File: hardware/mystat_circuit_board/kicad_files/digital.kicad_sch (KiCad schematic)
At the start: 28 parts, among them J2 2173157-3, P1 ICSP, U5 PIC16F1459, U6 ADR421, U7 MCP3551, U8 MCP3551, U9 DAC1220, X1 2.5 MHz

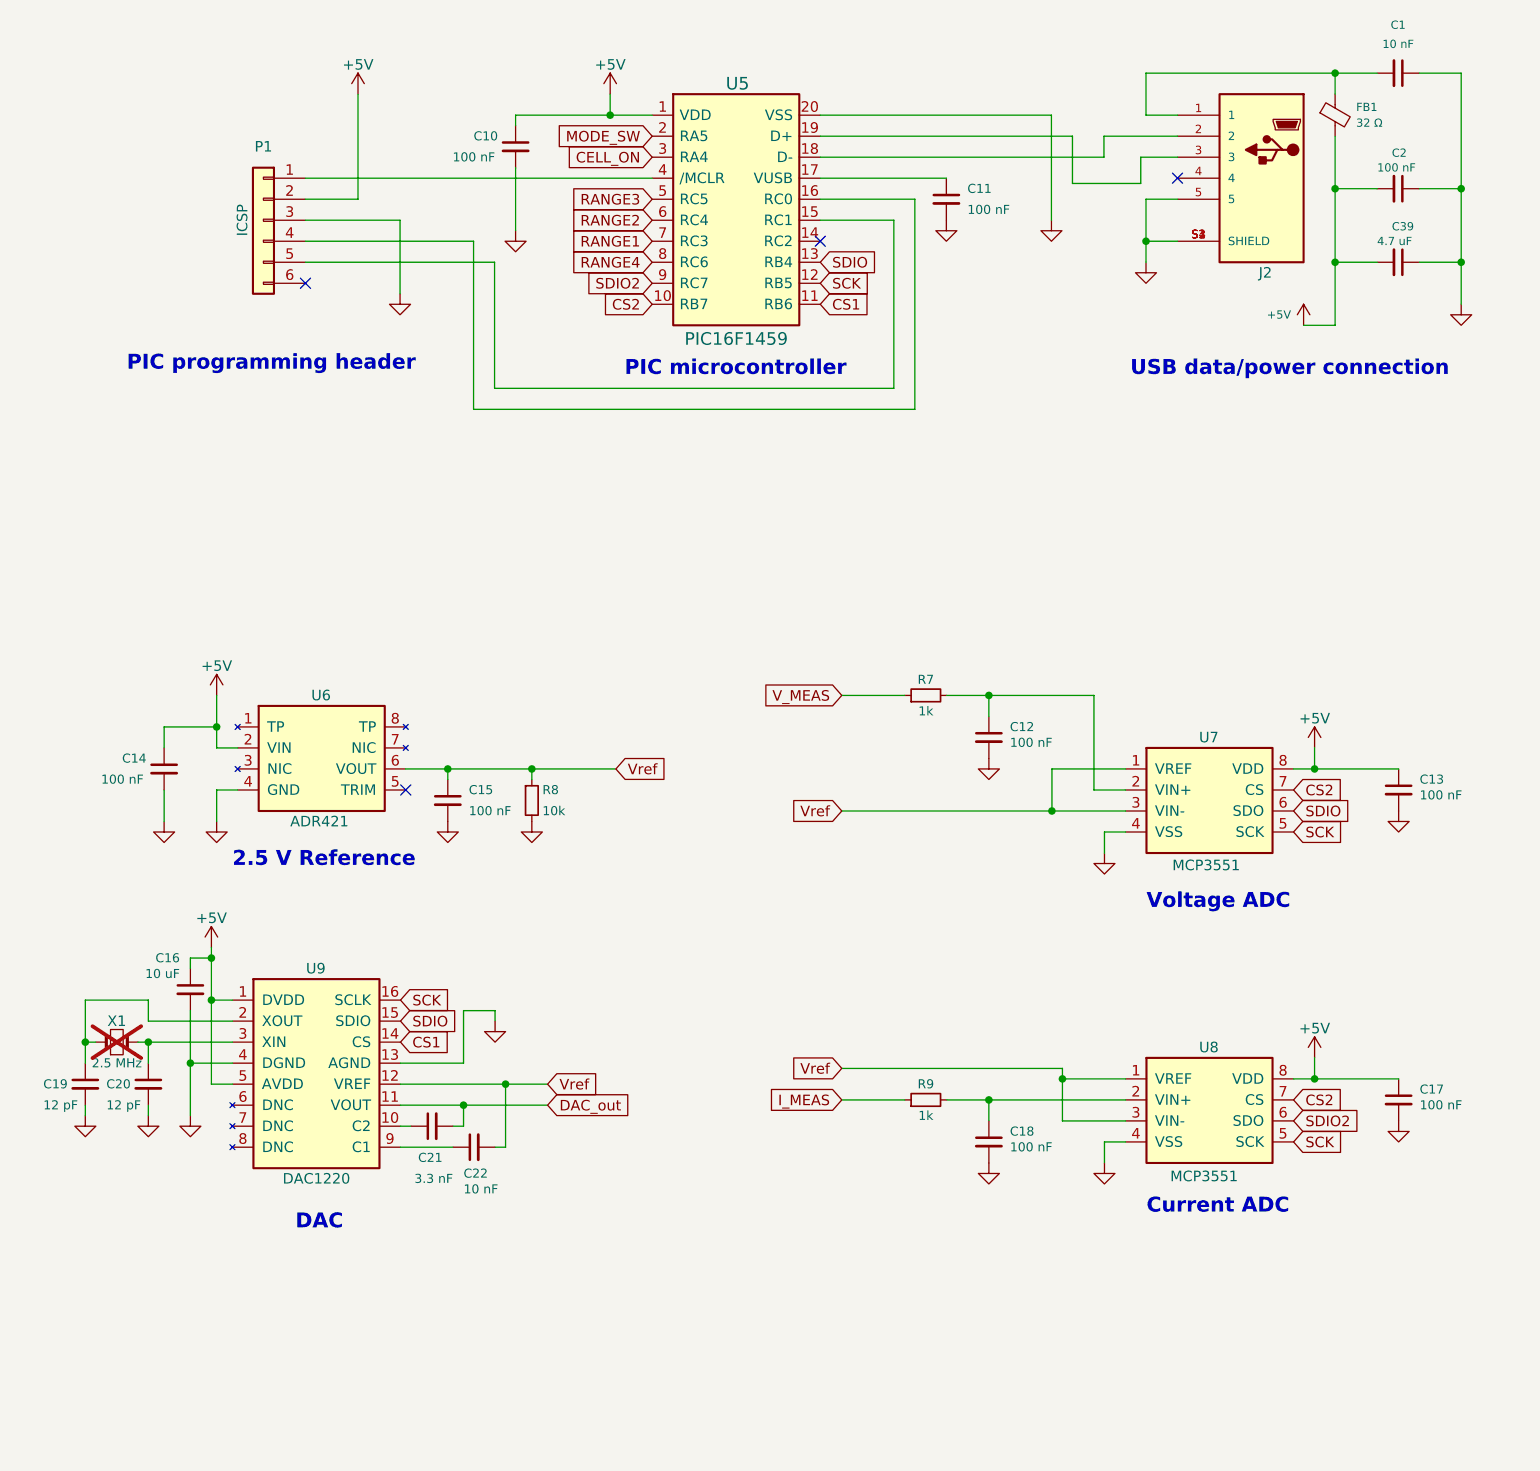
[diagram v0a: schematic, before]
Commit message: change micro USB to USB C 16P 2.0, rotate U11 for routing of thermal pad version
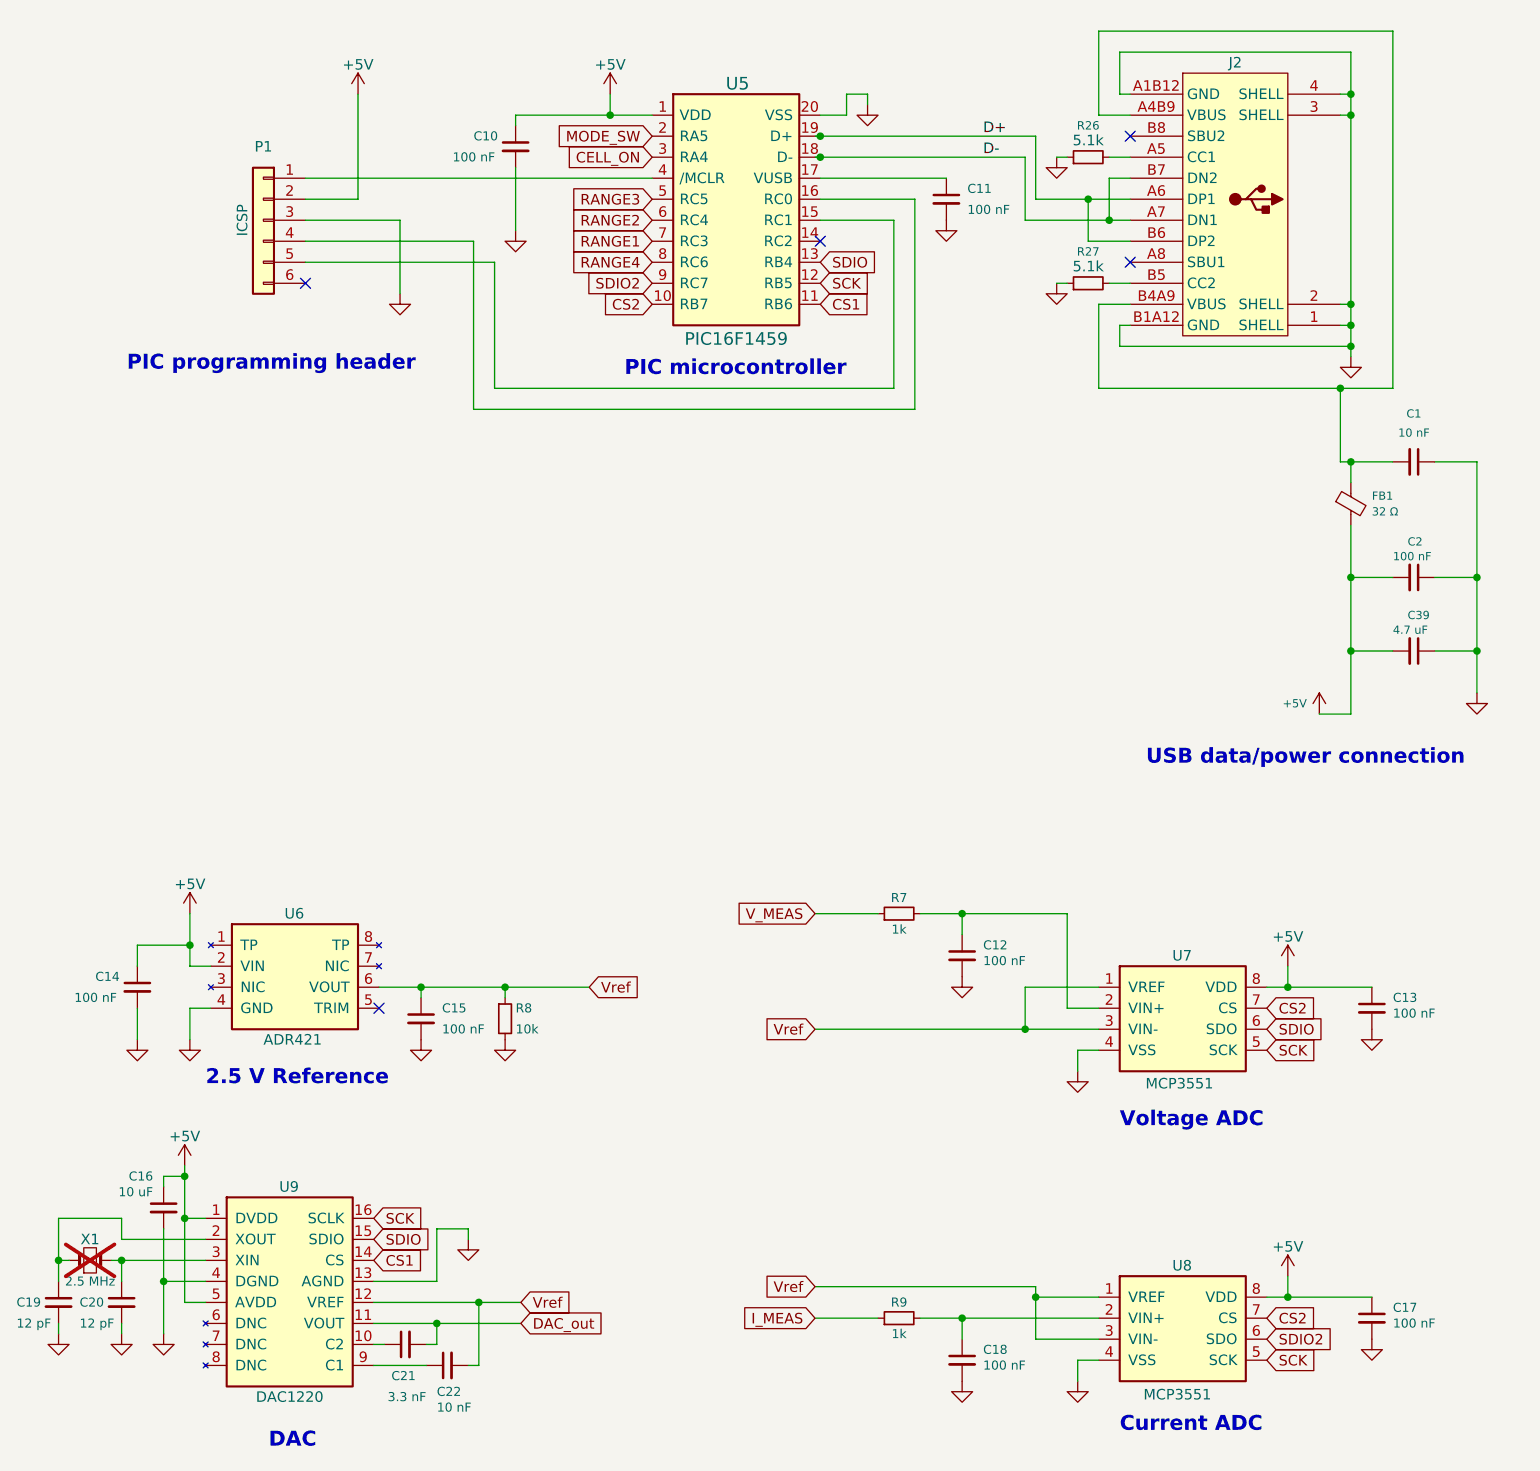
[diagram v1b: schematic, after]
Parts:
- removed J2: 2173157-3, my_footprints:CONN_2173157-3, symbol mylib:2173157-3
- added J2: (no value), my_footprints:USB_C_Receptacle_G-Switch_GT-USB-7010ASV, symbol mylib:G-Switch_GT-USB-7010ASV
- added R26, R27: 5.1k, Resistor_SMD:R_0805_2012Metric, symbol Device:R_Small
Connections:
- net GND: now also J2.1 (SHELL), J2.2 (SHELL), J2.3 (SHELL), J2.4 (SHELL), J2.A1B12 (GND), J2.B1A12 (GND), R26.1, R27.1
- net D-: now reaches U5.18 (D-)
- net D-: now also J2.A7 (DN1), J2.B7 (DN2)
- net D+: now reaches U5.19 (D+)
- net D+: now also J2.A6 (DP1), J2.B6 (DP2)
- net at C1.2, FB1.1: now also J2.A4B9 (VBUS), J2.B4A9 (VBUS)
- new net: J2.B5 (CC2), R27.2
- new net: J2.A5 (CC1), R26.2
- no-connect marks 4 -> 5
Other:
- moved on the sheet: C1, C12, C13, C14, C15, C16, C17, C18, C19, C2, C20, C21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

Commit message: more pcb layout progress save
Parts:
- C1, C22: MPN (none) -> C0805C103J5GACTU
- C10, C11, C12, C13, C14, C15, C17, C18, C2: MPN (none) -> 08055C104KAT2A
- C16: MPN (none) -> CL32B106KBJNNWE
- C19, C20: MPN (none) -> CC0805JRNPO9BN120
- C21: MPN (none) -> GRM2165C1H332JA01D
- C39: MPN (none) -> C2012X7R1V475K125AC
- FB1: value 32 Ω -> 33 Ω; LCSC Part (none) -> C50326194; LSCS Part (none) -> C50326194; MPN (none) -> APBH2012-330WTD16; Manufacturer Vishay Dale -> APV; Part Number * -> APBH2012-330WTD16
- J2: LCSC C2988369 -> (none); LCSC Part (none) -> C2988369; MFN GT-USB-7010ASV -> (none); MPN (none) -> GT-USB-7010ASV; Part Number (none) -> GT-USB-7010ASV
- P1: LCSC Part (none) -> C32713272; MPN (none) -> HX PZ2.54-1x6P ZZ; Manufacturer Sullins Connector Solutions -> hanxia; Part Number PRPC006SAAN-RC -> HX PZ2.54-1x6P ZZ
- R26, R27: LCSC C27834 -> (none); LCSC Part (none) -> C27834
- R7, R9: MPN (none) -> RC0805FR-071KL
- R8: MPN (none) -> RC0805FR-0710KL
- U5: MPN (none) -> PIC16F1459-I/SO
- U6: MPN (none) -> ADR421ARZ
- U7, U8: LCSC C1520170 -> (none); LCSC Part (none) -> C1520170; MPN (none) -> MCP3551-E/SN
- U9: MPN (none) -> DAC1220E
- X1: MPN (none) -> ECS-25-S-1X

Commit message: mostly resistor changes
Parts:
- C1, C22: LCSC Part (none) -> C2167597; Part Number C0805C103J5GACTU -> (none)
- C10, C11, C12, C13, C14, C15, C17, C18, C2: LCSC Part (none) -> C49678; MPN 08055C104KAT2A -> CC0805KRX7R9BB104; Manufacturer AVX Corporation -> YAGEO; Part Number 08055C104KAT2A -> (none)
- C16: footprint Capacitor_SMD:C_1210_3225Metric -> Capacitor_SMD:C_0805_2012Metric; LCSC Part (none) -> C15850; MPN CL32B106KBJNNWE -> CL21A106KAYNNNE; Part Number CL32B106KBJNNWE -> (none)
- C19, C20: footprint Capacitor_SMD:C_0805_2012Metric -> Capacitor_SMD:C_0603_1608Metric; LCSC Part (none) -> C38523; MPN CC0805JRNPO9BN120 -> CL10C120JB8NNNC; Manufacturer Yageo -> Samsung Electro-Mechanics; Part Number CC0805JRNPO9BN120 -> (none)
- C21: LCSC Part (none) -> C77062; Part Number GRM2165C1H332JA01D -> (none)
- C39: LCSC Part (none) -> C1779; MPN C2012X7R1V475K125AC -> CL21A475KAQNNNE; Manufacturer TDK Corporation -> Samsung Electro-Mechanics; Part Number C2012X7R1V475K125AC -> (none)
- FB1: LCSC Part C50326194 -> C6968654; LSCS Part C50326194 -> (none); MPN APBH2012-330WTD16 -> ILBB0805ER320V; Manufacturer APV -> Vishay Intertech; Part Number APBH2012-330WTD16 -> (none)
- J2: Part Number GT-USB-7010ASV -> (none)
- P1: Part Number HX PZ2.54-1x6P ZZ -> (none)
- R26, R27: MPN (none) -> 0805W8F5101T5E; Manufacturer (none) -> UNI-ROYAL
- R7, R9: LCSC Part (none) -> C95781; Part Number RC0805FR-071KL -> (none)
- R8: LCSC Part (none) -> C84376; Part Number RC0805FR-0710KL -> (none)
- U5: LCSC Part (none) -> C643250; Part Number PIC16F1459-I/SO -> (none)
- U6: LCSC Part (none) -> C9650; MPN ADR421ARZ -> ADR421ARZ-REEL7; Part Number ADR421ARZ -> (none)
- U7, U8: value MCP3551 -> MCP3551-E/SN; LCSC Part C1520170 -> C623293; MPN MCP3551-E/SN -> MCP3551T-E/SN; Part Number MCP3551-E/SN -> (none)
- U9: LCSC Part (none) -> C478450; Part Number DAC1220E -> (none)
- X1: Part Number ECS-25-S-1X -> (none)
